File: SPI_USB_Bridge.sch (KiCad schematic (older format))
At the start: 13 parts, among them P1 USB_A, U10 MAX3421, Y2 12MHz

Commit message: resolved ERC errors, and began assigning footprints
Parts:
- removed P1: USB_A, symbol USB_A
- added D7, D8: LED, symbol LED
- added J7: 48258-0001, symbol 48258-0001
- added Q2, Q3: IRLML2502, symbol IRLML2502
- added R77, R79: 1k, symbol R_Small
- added R78, R80: 37.5, symbol R_Small
- C100, C101, C104, C105: footprint (none) -> Capacitors_SMD:C_0603
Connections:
- net labels added: +3.3V
- net labels removed: +3.3V-RESCUE-DFTBoard
- wire segments 74 -> 84
- no-connect marks 4 -> 2
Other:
- moved on the sheet: C104, C105

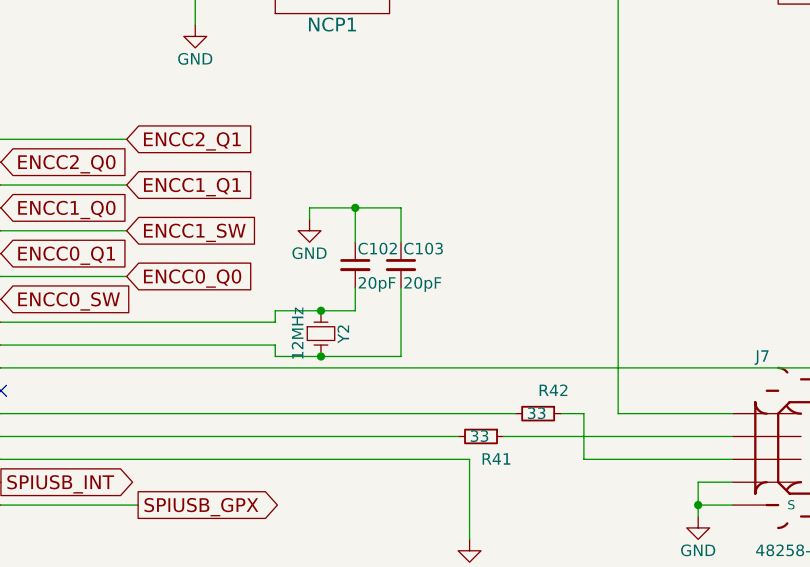
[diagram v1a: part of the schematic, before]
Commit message: finished assigning cap footprints
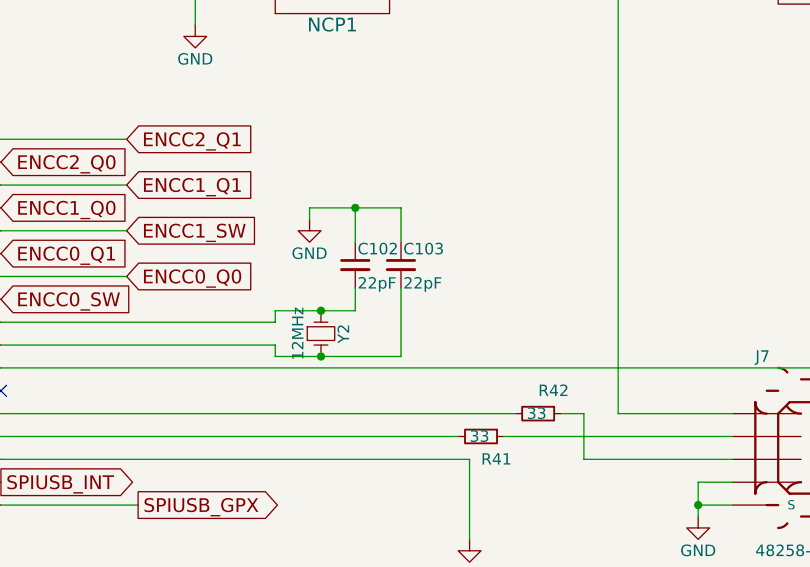
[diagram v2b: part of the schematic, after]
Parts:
- C102, C103: value 20pF -> 22pF; footprint (none) -> Capacitors_SMD:C_0201
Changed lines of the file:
@@
 $EndComp
 $Comp
-L +1.8V #PWR0103
+L +1.8V #PWR104
 U 1 1 5862C5D3
 P 1700 2700
-F 0 "#PWR0103" H 1700 2840 20  0001 C CNN
+F 0 "#PWR104" H 1700 2840 20  0001 C CNN
 F 1 "+1.8V" H 1700 2810 30  0000 C CNN
 F 2 "" H 1700 2700 60  0001 C CNN
@@
 $EndComp
 $Comp
-L GND #PWR0104
+L GND #PWR105
 U 1 1 5862C61D
 P 1700 3500
-F 0 "#PWR0104" H 1700 3250 50  0001 C CNN
+F 0 "#PWR105" H 1700 3250 50  0001 C CNN
 F 1 "GND" H 1700 3350 50  0000 C CNN
 F 2 "" H 1700 3500 50  0000 C CNN
@@
 $EndComp
 $Comp
-L GND #PWR0105
+L GND #PWR111
 U 1 1 5862C682
 P 7900 4850
-F 0 "#PWR0105" H 7900 4600 50  0001 C CNN
+F 0 "#PWR111" H 7900 4600 50  0001 C CNN
 F 1 "GND" H 7900 4700 50  0000 C CNN
 F 2 "" H 7900 4850 50  0000 C CNN
@@
 SPIUSB_GPX
 $Comp
-L GND #PWR0106
+L GND #PWR112
 U 1 1 5862D1A5
 P 8900 4750
-F 0 "#PWR0106" H 8900 4500 50  0001 C CNN
+F 0 "#PWR112" H 8900 4500 50  0001 C CNN
 F 1 "GND" H 8900 4600 50  0000 C CNN
 F 2 "" H 8900 4750 50  0000 C CNN
@@
 $EndComp
 $Comp
-L GND #PWR0107
+L GND #PWR115
 U 1 1 5862D52A
 P 10900 4700
-F 0 "#PWR0107" H 10900 4450 50  0001 C CNN
+F 0 "#PWR115" H 10900 4450 50  0001 C CNN
 F 1 "GND" H 10900 4550 50  0000 C CNN
 F 2 "" H 10900 4700 50  0000 C CNN
@@
 P 7400 3650
 F 0 "C102" H 7410 3720 50  0000 L CNN
-F 1 "20pF" H 7410 3570 50  0000 L CNN
-F 2 "" H 7400 3650 50  0001 C CNN
+F 1 "22pF" H 7410 3570 50  0000 L CNN
+F 2 "Capacitors_SMD:C_0201" H 7400 3650 50  0001 C CNN
 F 3 "" H 7400 3650 50  0000 C CNN
 	1    7400 3650
@@
 P 7600 3650
 F 0 "C103" H 7610 3720 50  0000 L CNN
-F 1 "20pF" H 7610 3570 50  0000 L CNN
-F 2 "" H 7600 3650 50  0001 C CNN
+F 1 "22pF" H 7610 3570 50  0000 L CNN
+F 2 "Capacitors_SMD:C_0201" H 7600 3650 50  0001 C CNN
 F 3 "" H 7600 3650 50  0000 C CNN
 	1    7600 3650
@@
 $EndComp
 $Comp
-L GND #PWR0108
+L GND #PWR110
 U 1 1 5862DAA7
 P 7200 3450
-F 0 "#PWR0108" H 7200 3200 50  0001 C CNN
+F 0 "#PWR110" H 7200 3200 50  0001 C CNN
 F 1 "GND" H 7200 3300 50  0000 C CNN
 F 2 "" H 7200 3450 50  0000 C CNN
@@
 $EndComp
 $Comp
-L +5V #PWR0109
+L +5V #PWR108
 U 1 1 5862DFFF
 P 6600 2050
-F 0 "#PWR0109" H 6600 1900 50  0001 C CNN
+F 0 "#PWR108" H 6600 1900 50  0001 C CNN
 F 1 "+5V" H 6600 2190 50  0000 C CNN
 F 2 "" H 6600 2050 50  0000 C CNN
@@
 $EndComp
 $Comp
-L GND #PWR0110
+L GND #PWR109
 U 1 1 5862E157
 P 6700 2600
-F 0 "#PWR0110" H 6700 2350 50  0001 C CNN
+F 0 "#PWR109" H 6700 2350 50  0001 C CNN
 F 1 "GND" H 6700 2450 50  0000 C CNN
 F 2 "" H 6700 2600 50  0000 C CNN
@@
 	8950 2450 8950 2350
 $Comp
-L +5V #PWR0111
+L +5V #PWR113
 U 1 1 5862E815
 P 8950 1950
-F 0 "#PWR0111" H 8950 1800 50  0001 C CNN
+F 0 "#PWR113" H 8950 1800 50  0001 C CNN
 F 1 "+5V" H 8950 2090 50  0000 C CNN
 F 2 "" H 8950 1950 50  0000 C CNN
@@
 	2150 4100 2150 5400
 $Comp
-L GND #PWR0112
+L GND #PWR103
 U 1 1 586FEB40
 P 1650 5600
-F 0 "#PWR0112" H 1650 5350 50  0001 C CNN
+F 0 "#PWR103" H 1650 5350 50  0001 C CNN
 F 1 "GND" H 1650 5450 50  0000 C CNN
 F 2 "" H 1650 5600 50  0000 C CNN
@@
 $EndComp
 $Comp
-L GND #PWR0113
+L GND #PWR107
 U 1 1 586FEDFD
 P 2800 5600
-F 0 "#PWR0113" H 2800 5350 50  0001 C CNN
+F 0 "#PWR107" H 2800 5350 50  0001 C CNN
 F 1 "GND" H 2800 5450 50  0000 C CNN
 F 2 "" H 2800 5600 50  0000 C CNN
@@
 	1650 4650 1650 4550
 $Comp
-L +5V #PWR0114
+L +5V #PWR102
 U 1 1 58700335
 P 1650 4250
-F 0 "#PWR0114" H 1650 4100 50  0001 C CNN
+F 0 "#PWR102" H 1650 4100 50  0001 C CNN
 F 1 "+5V" H 1650 4390 50  0000 C CNN
 F 2 "" H 1650 4250 50  0000 C CNN
@@
 	1650 4250 1650 4350
 $Comp
-L +5V #PWR0115
+L +5V #PWR106
 U 1 1 58700402
 P 2800 4300
-F 0 "#PWR0115" H 2800 4150 50  0001 C CNN
+F 0 "#PWR106" H 2800 4150 50  0001 C CNN
 F 1 "+5V" H 2800 4440 50  0000 C CNN
 F 2 "" H 2800 4300 50  0000 C CNN
@@
 	6450 4700 5850 4700
 $Comp
-L +3.3V #PWR0116
+L +3.3V #PWR114
 U 1 1 58742C2F
 P 10750 4100
-F 0 "#PWR0116" H 10750 3950 50  0001 C CNN
+F 0 "#PWR114" H 10750 3950 50  0001 C CNN
 F 1 "+3.3V" H 10750 4240 50  0000 C CNN
 F 2 "" H 10750 4100 50  0000 C CNN

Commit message: a few more footprints
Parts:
- D7: value LED -> LED RED; footprint (none) -> LEDs:LED_0603
- D8: value LED -> LED BLUE; footprint (none) -> LEDs:LED_0603
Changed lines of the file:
@@
 $EndComp
 $Comp
-L +1.8V #PWR104
+L +1.8V #PWR0103
 U 1 1 5862C5D3
 P 1700 2700
-F 0 "#PWR104" H 1700 2840 20  0001 C CNN
+F 0 "#PWR0103" H 1700 2840 20  0001 C CNN
 F 1 "+1.8V" H 1700 2810 30  0000 C CNN
 F 2 "" H 1700 2700 60  0001 C CNN
@@
 $EndComp
 $Comp
-L GND #PWR105
+L GND #PWR0104
 U 1 1 5862C61D
 P 1700 3500
-F 0 "#PWR105" H 1700 3250 50  0001 C CNN
+F 0 "#PWR0104" H 1700 3250 50  0001 C CNN
 F 1 "GND" H 1700 3350 50  0000 C CNN
 F 2 "" H 1700 3500 50  0000 C CNN
@@
 $EndComp
 $Comp
-L GND #PWR111
+L GND #PWR0105
 U 1 1 5862C682
 P 7900 4850
-F 0 "#PWR111" H 7900 4600 50  0001 C CNN
+F 0 "#PWR0105" H 7900 4600 50  0001 C CNN
 F 1 "GND" H 7900 4700 50  0000 C CNN
 F 2 "" H 7900 4850 50  0000 C CNN
@@
 SPIUSB_GPX
 $Comp
-L GND #PWR112
+L GND #PWR0106
 U 1 1 5862D1A5
 P 8900 4750
-F 0 "#PWR112" H 8900 4500 50  0001 C CNN
+F 0 "#PWR0106" H 8900 4500 50  0001 C CNN
 F 1 "GND" H 8900 4600 50  0000 C CNN
 F 2 "" H 8900 4750 50  0000 C CNN
@@
 $EndComp
 $Comp
-L GND #PWR115
+L GND #PWR0107
 U 1 1 5862D52A
 P 10900 4700
-F 0 "#PWR115" H 10900 4450 50  0001 C CNN
+F 0 "#PWR0107" H 10900 4450 50  0001 C CNN
 F 1 "GND" H 10900 4550 50  0000 C CNN
 F 2 "" H 10900 4700 50  0000 C CNN
@@
 $EndComp
 $Comp
-L GND #PWR110
+L GND #PWR0108
 U 1 1 5862DAA7
 P 7200 3450
-F 0 "#PWR110" H 7200 3200 50  0001 C CNN
+F 0 "#PWR0108" H 7200 3200 50  0001 C CNN
 F 1 "GND" H 7200 3300 50  0000 C CNN
 F 2 "" H 7200 3450 50  0000 C CNN
@@
 $EndComp
 $Comp
-L +5V #PWR108
+L +5V #PWR0109
 U 1 1 5862DFFF
 P 6600 2050
-F 0 "#PWR108" H 6600 1900 50  0001 C CNN
+F 0 "#PWR0109" H 6600 1900 50  0001 C CNN
 F 1 "+5V" H 6600 2190 50  0000 C CNN
 F 2 "" H 6600 2050 50  0000 C CNN
@@
 $EndComp
 $Comp
-L GND #PWR109
+L GND #PWR0110
 U 1 1 5862E157
 P 6700 2600
-F 0 "#PWR109" H 6700 2350 50  0001 C CNN
+F 0 "#PWR0110" H 6700 2350 50  0001 C CNN
 F 1 "GND" H 6700 2450 50  0000 C CNN
 F 2 "" H 6700 2600 50  0000 C CNN
@@
 	8950 2450 8950 2350
 $Comp
-L +5V #PWR113
+L +5V #PWR0111
 U 1 1 5862E815
 P 8950 1950
-F 0 "#PWR113" H 8950 1800 50  0001 C CNN
+F 0 "#PWR0111" H 8950 1800 50  0001 C CNN
 F 1 "+5V" H 8950 2090 50  0000 C CNN
 F 2 "" H 8950 1950 50  0000 C CNN
@@
 	2150 4100 2150 5400
 $Comp
-L GND #PWR103
+L GND #PWR0112
 U 1 1 586FEB40
 P 1650 5600
-F 0 "#PWR103" H 1650 5350 50  0001 C CNN
+F 0 "#PWR0112" H 1650 5350 50  0001 C CNN
 F 1 "GND" H 1650 5450 50  0000 C CNN
 F 2 "" H 1650 5600 50  0000 C CNN
@@
 $EndComp
 $Comp
-L GND #PWR107
+L GND #PWR0113
 U 1 1 586FEDFD
 P 2800 5600
-F 0 "#PWR107" H 2800 5350 50  0001 C CNN
+F 0 "#PWR0113" H 2800 5350 50  0001 C CNN
 F 1 "GND" H 2800 5450 50  0000 C CNN
 F 2 "" H 2800 5600 50  0000 C CNN
@@
 P 1650 4850
 F 0 "D7" H 1650 4950 50  0000 C CNN
-F 1 "LED" H 1650 4750 50  0000 C CNN
-F 2 "" H 1650 4850 50  0001 C CNN
+F 1 "LED RED" H 1650 4750 50  0000 C CNN
+F 2 "LEDs:LED_0603" H 1650 4850 50  0001 C CNN
 F 3 "" H 1650 4850 50  0000 C CNN
 	1    1650 4850
@@
 P 2800 4850
 F 0 "D8" H 2800 4950 50  0000 C CNN
-F 1 "LED" H 2800 4750 50  0000 C CNN
-F 2 "" H 2800 4850 50  0001 C CNN
+F 1 "LED BLUE" H 2800 4750 50  0000 C CNN
+F 2 "LEDs:LED_0603" H 2800 4850 50  0001 C CNN
 F 3 "" H 2800 4850 50  0000 C CNN
 	1    2800 4850
@@
 	1650 4650 1650 4550
 $Comp
-L +5V #PWR102
+L +5V #PWR0114
 U 1 1 58700335
 P 1650 4250
-F 0 "#PWR102" H 1650 4100 50  0001 C CNN
+F 0 "#PWR0114" H 1650 4100 50  0001 C CNN
 F 1 "+5V" H 1650 4390 50  0000 C CNN
 F 2 "" H 1650 4250 50  0000 C CNN
@@
 	1650 4250 1650 4350
 $Comp
-L +5V #PWR106
+L +5V #PWR0115
 U 1 1 58700402
 P 2800 4300
-F 0 "#PWR106" H 2800 4150 50  0001 C CNN
+F 0 "#PWR0115" H 2800 4150 50  0001 C CNN
 F 1 "+5V" H 2800 4440 50  0000 C CNN
 F 2 "" H 2800 4300 50  0000 C CNN
@@
 	6450 4700 5850 4700
 $Comp
-L +3.3V #PWR114
+L +3.3V #PWR0116
 U 1 1 58742C2F
 P 10750 4100
-F 0 "#PWR114" H 10750 3950 50  0001 C CNN
+F 0 "#PWR0116" H 10750 3950 50  0001 C CNN
 F 1 "+3.3V" H 10750 4240 50  0000 C CNN
 F 2 "" H 10750 4100 50  0000 C CNN

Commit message: A few more footprints
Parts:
- J7: footprint (none) -> 48258-0001:MOLEX_48258-0001
- NCP1: footprint (none) -> UDFN-6:UDFN-6
- U10: footprint (none) -> TQFP32-5MM:TQFP32-5MM
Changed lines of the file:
@@
 F 0 "U10" H 5000 4250 60  0000 C CNN
 F 1 "MAX3421" H 5000 3550 60  0000 C CNN
-F 2 "" H 5000 3550 60  0001 C CNN
+F 2 "TQFP32-5MM:TQFP32-5MM" H 5000 3550 60  0001 C CNN
 F 3 "" H 5000 3550 60  0000 C CNN
 	1    5000 3950
@@
 F 0 "NCP1" H 7300 2100 60  0000 C CNN
 F 1 "NCP361" H 7300 2600 60  0000 C CNN
-F 2 "" H 6900 2350 60  0001 C CNN
+F 2 "UDFN-6:UDFN-6" H 6900 2350 60  0001 C CNN
 F 3 "" H 6900 2350 60  0000 C CNN
 	1    7300 2350
@@
 F 0 "J7" H 9150 4950 50  0000 L CNN
 F 1 "48258-0001" H 9150 4100 50  0000 L CNN
-F 2 "" H 9250 4500 50  0001 L CNN
+F 2 "48258-0001:MOLEX_48258-0001" H 9250 4500 50  0001 L CNN
 F 3 "Molex" H 9250 4500 50  0001 L CNN
 F 4 "None" H 9250 4500 50  0001 L CNN "Package"

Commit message: forgot to save sch
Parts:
- Q2, Q3: footprint (none) -> TO_SOT_Packages_SMD:SOT-23
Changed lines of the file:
@@
 F 0 "Q2" H 1550 5201 40  0000 R CNN
 F 1 "IRLML2502" H 1550 5500 40  0000 R CNN
-F 2 "" H 1420 5452 29  0001 C CNN
+F 2 "TO_SOT_Packages_SMD:SOT-23" H 1420 5452 29  0001 C CNN
 F 3 "" H 1550 5350 60  0000 C CNN
 	1    1550 5350
@@
 F 0 "Q3" H 2700 5201 40  0000 R CNN
 F 1 "IRLML2502" H 2700 5500 40  0000 R CNN
-F 2 "" H 2570 5452 29  0001 C CNN
+F 2 "TO_SOT_Packages_SMD:SOT-23" H 2570 5452 29  0001 C CNN
 F 3 "" H 2700 5350 60  0000 C CNN
 	1    2700 5350

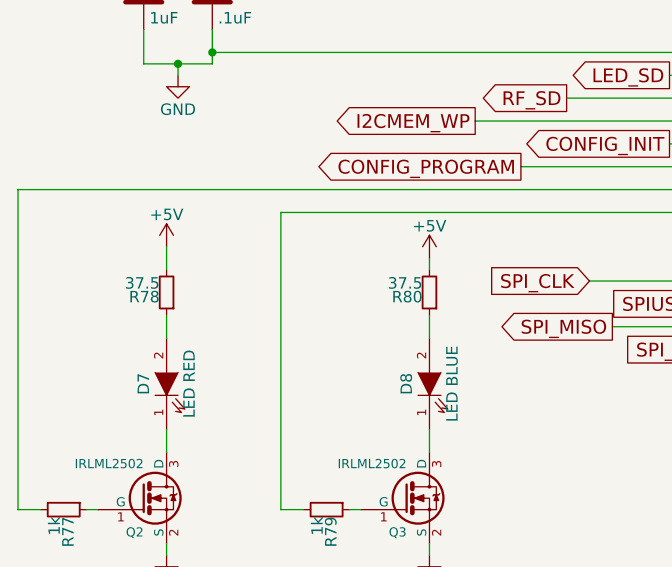
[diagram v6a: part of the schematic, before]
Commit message: edited LED resistor values
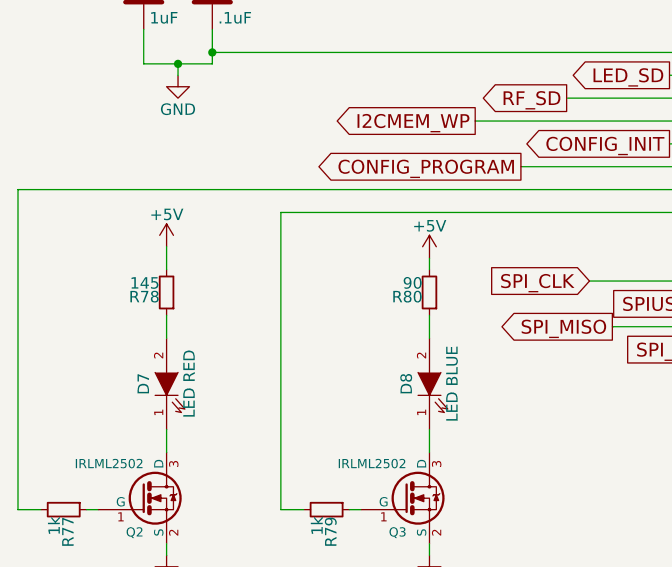
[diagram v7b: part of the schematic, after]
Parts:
- R78: value 37.5 -> 145
- R80: value 37.5 -> 90
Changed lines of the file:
@@
 $EndComp
 $Comp
-L +1.8V #PWR105
+L +1.8V #PWR0104
 U 1 1 5862C5D3
 P 1700 2700
-F 0 "#PWR105" H 1700 2840 20  0001 C CNN
+F 0 "#PWR0104" H 1700 2840 20  0001 C CNN
 F 1 "+1.8V" H 1700 2810 30  0000 C CNN
 F 2 "" H 1700 2700 60  0001 C CNN
@@
 $EndComp
 $Comp
-L GND #PWR106
+L GND #PWR0105
 U 1 1 5862C61D
 P 1700 3500
-F 0 "#PWR106" H 1700 3250 50  0001 C CNN
+F 0 "#PWR0105" H 1700 3250 50  0001 C CNN
 F 1 "GND" H 1700 3350 50  0000 C CNN
 F 2 "" H 1700 3500 50  0000 C CNN
@@
 $EndComp
 $Comp
-L GND #PWR112
+L GND #PWR0106
 U 1 1 5862C682
 P 7900 4850
-F 0 "#PWR112" H 7900 4600 50  0001 C CNN
+F 0 "#PWR0106" H 7900 4600 50  0001 C CNN
 F 1 "GND" H 7900 4700 50  0000 C CNN
 F 2 "" H 7900 4850 50  0000 C CNN
@@
 SPIUSB_GPX
 $Comp
-L GND #PWR113
+L GND #PWR0107
 U 1 1 5862D1A5
 P 8900 4750
-F 0 "#PWR113" H 8900 4500 50  0001 C CNN
+F 0 "#PWR0107" H 8900 4500 50  0001 C CNN
 F 1 "GND" H 8900 4600 50  0000 C CNN
 F 2 "" H 8900 4750 50  0000 C CNN
@@
 $EndComp
 $Comp
-L GND #PWR116
+L GND #PWR0108
 U 1 1 5862D52A
 P 10900 4700
-F 0 "#PWR116" H 10900 4450 50  0001 C CNN
+F 0 "#PWR0108" H 10900 4450 50  0001 C CNN
 F 1 "GND" H 10900 4550 50  0000 C CNN
 F 2 "" H 10900 4700 50  0000 C CNN
@@
 $EndComp
 $Comp
-L GND #PWR111
+L GND #PWR0109
 U 1 1 5862DAA7
 P 7200 3450
-F 0 "#PWR111" H 7200 3200 50  0001 C CNN
+F 0 "#PWR0109" H 7200 3200 50  0001 C CNN
 F 1 "GND" H 7200 3300 50  0000 C CNN
 F 2 "" H 7200 3450 50  0000 C CNN
@@
 $EndComp
 $Comp
-L +5V #PWR109
+L +5V #PWR0110
 U 1 1 5862DFFF
 P 6600 2050
-F 0 "#PWR109" H 6600 1900 50  0001 C CNN
+F 0 "#PWR0110" H 6600 1900 50  0001 C CNN
 F 1 "+5V" H 6600 2190 50  0000 C CNN
 F 2 "" H 6600 2050 50  0000 C CNN
@@
 $EndComp
 $Comp
-L GND #PWR110
+L GND #PWR0111
 U 1 1 5862E157
 P 6700 2600
-F 0 "#PWR110" H 6700 2350 50  0001 C CNN
+F 0 "#PWR0111" H 6700 2350 50  0001 C CNN
 F 1 "GND" H 6700 2450 50  0000 C CNN
 F 2 "" H 6700 2600 50  0000 C CNN
@@
 	8950 2450 8950 2350
 $Comp
-L +5V #PWR114
+L +5V #PWR0112
 U 1 1 5862E815
 P 8950 1950
-F 0 "#PWR114" H 8950 1800 50  0001 C CNN
+F 0 "#PWR0112" H 8950 1800 50  0001 C CNN
 F 1 "+5V" H 8950 2090 50  0000 C CNN
 F 2 "" H 8950 1950 50  0000 C CNN
@@
 	2150 4100 2150 5400
 $Comp
-L GND #PWR104
+L GND #PWR0113
 U 1 1 586FEB40
 P 1650 5600
-F 0 "#PWR104" H 1650 5350 50  0001 C CNN
+F 0 "#PWR0113" H 1650 5350 50  0001 C CNN
 F 1 "GND" H 1650 5450 50  0000 C CNN
 F 2 "" H 1650 5600 50  0000 C CNN
@@
 $EndComp
 $Comp
-L GND #PWR108
+L GND #PWR0114
 U 1 1 586FEDFD
 P 2800 5600
-F 0 "#PWR108" H 2800 5350 50  0001 C CNN
+F 0 "#PWR0114" H 2800 5350 50  0001 C CNN
 F 1 "GND" H 2800 5450 50  0000 C CNN
 F 2 "" H 2800 5600 50  0000 C CNN
@@
 P 1650 4450
 F 0 "R78" H 1680 4470 50  0000 L CNN
-F 1 "37.5" H 1680 4410 50  0000 L CNN
+F 1 "145" H 1680 4410 50  0000 L CNN
 F 2 "" H 1650 4450 50  0001 C CNN
 F 3 "" H 1650 4450 50  0000 C CNN
@@
 P 2800 4450
 F 0 "R80" H 2830 4470 50  0000 L CNN
-F 1 "37.5" H 2830 4410 50  0000 L CNN
+F 1 "90" H 2830 4410 50  0000 L CNN
 F 2 "" H 2800 4450 50  0001 C CNN
 F 3 "" H 2800 4450 50  0000 C CNN
@@
 	1650 4650 1650 4550
 $Comp
-L +5V #PWR103
+L +5V #PWR0115
 U 1 1 58700335
 P 1650 4250
-F 0 "#PWR103" H 1650 4100 50  0001 C CNN
+F 0 "#PWR0115" H 1650 4100 50  0001 C CNN
 F 1 "+5V" H 1650 4390 50  0000 C CNN
 F 2 "" H 1650 4250 50  0000 C CNN
@@
 	1650 4250 1650 4350
 $Comp
-L +5V #PWR107
+L +5V #PWR0116
 U 1 1 58700402
 P 2800 4300
-F 0 "#PWR107" H 2800 4150 50  0001 C CNN
+F 0 "#PWR0116" H 2800 4150 50  0001 C CNN
 F 1 "+5V" H 2800 4440 50  0000 C CNN
 F 2 "" H 2800 4300 50  0000 C CNN
@@
 	6450 4700 5850 4700
 $Comp
-L +3.3V #PWR115
+L +3.3V #PWR0117
 U 1 1 58742C2F
 P 10750 4100
-F 0 "#PWR115" H 10750 3950 50  0001 C CNN
+F 0 "#PWR0117" H 10750 3950 50  0001 C CNN
 F 1 "+3.3V" H 10750 4240 50  0000 C CNN
 F 2 "" H 10750 4100 50  0000 C CNN

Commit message: added resistor footprints (1206)
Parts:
- R41, R42, R43, R77, R78, R79, R80: footprint (none) -> Resistors_SMD:R_1206
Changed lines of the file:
@@
 F 0 "R42" V 8100 4300 50  0000 L CNN
 F 1 "33" V 8200 4250 50  0000 L CNN
-F 2 "" H 8200 4300 50  0001 C CNN
+F 2 "Resistors_SMD:R_1206" H 8200 4300 50  0001 C CNN
 F 3 "" H 8200 4300 50  0000 C CNN
 	1    8200 4300
@@
 F 0 "R41" V 8050 4400 50  0000 L CNN
 F 1 "33" V 7950 4350 50  0000 L CNN
-F 2 "" H 7950 4400 50  0001 C CNN
+F 2 "Resistors_SMD:R_1206" H 7950 4400 50  0001 C CNN
 F 3 "" H 7950 4400 50  0000 C CNN
 	1    7950 4400
@@
 F 0 "R43" V 9030 2200 50  0000 C CNN
 F 1 "20k" V 8950 2200 50  0000 C CNN
-F 2 "" V 8880 2200 50  0001 C CNN
+F 2 "Resistors_SMD:R_1206" V 8880 2200 50  0001 C CNN
 F 3 "" H 8950 2200 50  0000 C CNN
 	1    8950 2200
@@
 F 0 "R77" H 1230 5420 50  0000 L CNN
 F 1 "1k" H 1230 5360 50  0000 L CNN
-F 2 "" H 1200 5400 50  0001 C CNN
+F 2 "Resistors_SMD:R_1206" H 1200 5400 50  0001 C CNN
 F 3 "" H 1200 5400 50  0000 C CNN
 	1    1200 5400
@@
 F 0 "R79" H 2380 5420 50  0000 L CNN
 F 1 "1k" H 2380 5360 50  0000 L CNN
-F 2 "" H 2350 5400 50  0001 C CNN
+F 2 "Resistors_SMD:R_1206" H 2350 5400 50  0001 C CNN
 F 3 "" H 2350 5400 50  0000 C CNN
 	1    2350 5400
@@
 F 0 "R78" H 1680 4470 50  0000 L CNN
 F 1 "145" H 1680 4410 50  0000 L CNN
-F 2 "" H 1650 4450 50  0001 C CNN
+F 2 "Resistors_SMD:R_1206" H 1650 4450 50  0001 C CNN
 F 3 "" H 1650 4450 50  0000 C CNN
 	1    1650 4450
@@
 F 0 "R80" H 2830 4470 50  0000 L CNN
 F 1 "90" H 2830 4410 50  0000 L CNN
-F 2 "" H 2800 4450 50  0001 C CNN
+F 2 "Resistors_SMD:R_1206" H 2800 4450 50  0001 C CNN
 F 3 "" H 2800 4450 50  0000 C CNN
 	1    2800 4450
